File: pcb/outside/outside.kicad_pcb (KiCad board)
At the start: 2 copper layers, 56 parts, among them J1 USB_C_Receptacle_USB2.0_16P, J2 RJ12, J3 Conn_01x08, J4 Conn_01x04, Q1 NMOS, SW1 RST, SW2 PRG, U1 ESP32-C6-MINI-1, U2 MFRC52201HN1,157, U3 USBLC6-2P6, U4 AMS1117-3.3, Y1 XRCGB27M120F3M13R0

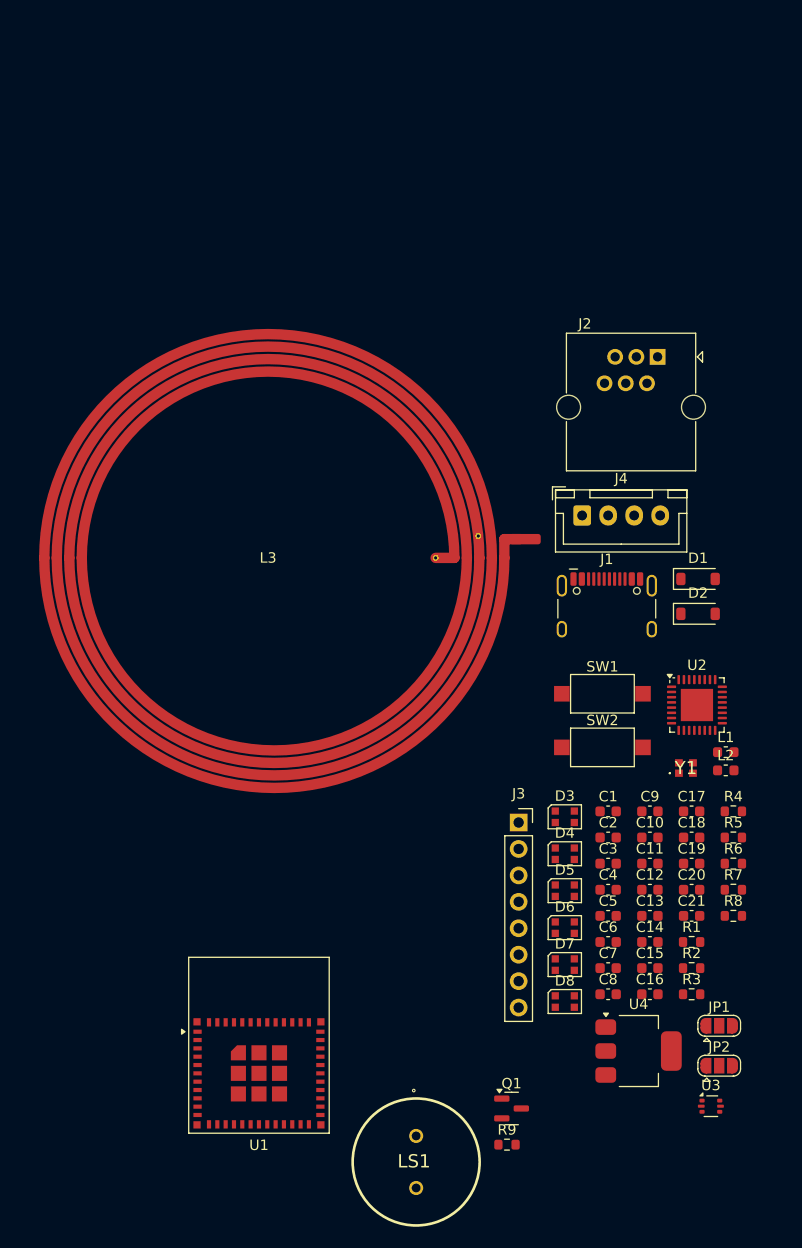
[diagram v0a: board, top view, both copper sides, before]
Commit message: feat: improve and rearrange schematic
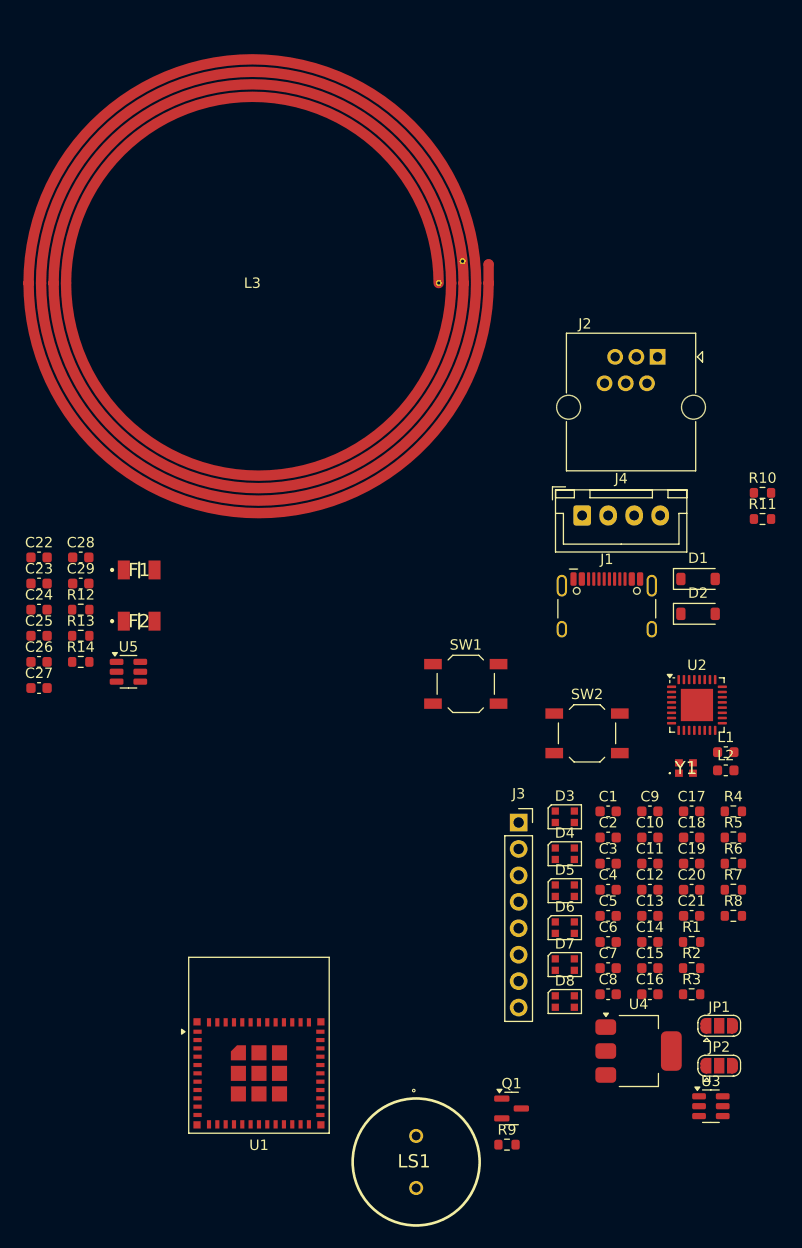
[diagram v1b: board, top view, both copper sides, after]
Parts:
- added C22: 100n, Capacitor_SMD:C_0603_1608Metric, F.Cu at (98.0, 76.5)
- added C23: 100n, Capacitor_SMD:C_0603_1608Metric, F.Cu at (98.0, 79.0)
- added C24: 100n, Capacitor_SMD:C_0603_1608Metric, F.Cu at (98.0, 81.5)
- added C25: 100n, Capacitor_SMD:C_0603_1608Metric, F.Cu at (98.0, 84.0)
- added C26: 100n, Capacitor_SMD:C_0603_1608Metric, F.Cu at (98.0, 86.5)
- added C27: 100n, Capacitor_SMD:C_0603_1608Metric, F.Cu at (98.0, 89.0)
- added C28: 100n, Capacitor_SMD:C_0603_1608Metric, F.Cu at (102.0, 76.5)
- added C29: 100n, Capacitor_SMD:C_0603_1608Metric, F.Cu at (102.0, 79.0)
- added F1: 500mA, belepteto:1206L05015YR, F.Cu at (107.6, 77.7)
- added F2: 500mA, belepteto:1206L05015YR, F.Cu at (107.6, 82.6)
- added R10: 5k1, Resistor_SMD:R_0603_1608Metric, F.Cu at (167.5, 70.3)
- added R11: 5k1, Resistor_SMD:R_0603_1608Metric, F.Cu at (167.5, 72.8)
- added R12: 180, Resistor_SMD:R_0603_1608Metric, F.Cu at (102.0, 81.5)
- added R13: 22, Resistor_SMD:R_0603_1608Metric, F.Cu at (102.0, 84.0)
- added R14: 22, Resistor_SMD:R_0603_1608Metric, F.Cu at (102.0, 86.5)
- added U5: USBLC6-2SC6, Package_TO_SOT_SMD:SOT-23-6, F.Cu at (106.6, 87.4)
- L1, L2: value 2.2uH -> 2u2
- L3: value 1.22uH -> 1u22
- LS1: value Speaker_Crystal -> PS1240P02BT
- Q1: value NMOS -> BSS138
- SW1, SW2: footprint Button_Switch_SMD:SW_SPST_CK_RS282G05A3 -> Button_Switch_SMD:SW_SPST_TL3342
- U3: value USBLC6-2P6 -> USBLC6-2SC6; footprint Package_TO_SOT_SMD:SOT-666 -> Package_TO_SOT_SMD:SOT-23-6
- Y1: value XRCGB27M120F3M13R0 -> 27.12MHz
- moved L3 26.4 mm to (118.5, 50.1)
- moved SW1 13.2 mm to (139.0, 88.6)
- moved SW2 2.00 mm to (150.6, 93.4)
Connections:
- net /EA renamed /RFID/EA
- net /I2C renamed /RFID/I2C
- net /IO2 renamed /ESP/SCLK
- net /IO3 renamed /ESP/MOSI
- net /IO4 renamed /ESP/MISO
- net /IO5 renamed /ESP/CS
- net /PRG renamed /ESP/PRG
- net Net-(J3-Pin_1) renamed /ESP/EXT_CS
- net Net-(J3-Pin_2) renamed /ESP/EXT_SCLK
- net Net-(J3-Pin_3) renamed /ESP/EXT_MOSI
- net Net-(J3-Pin_4) renamed /ESP/EXT_MISO
- net Net-(U2-OSCIN) renamed /RFID/OSC2
- net Net-(U2-OSCOUT) renamed /RFID/OSC1
- net Net-(U2-RX) renamed /RFID/RX
- net Net-(U2-TX1) renamed /RFID/TX1
- net Net-(U2-TX2) renamed /RFID/TX2
- net Net-(U2-VMID) renamed /RFID/VMID
- J1 pad A4: Net-(D1-A) -> Net-(F1-Pad1)
- J1 pad A9: Net-(D1-A) -> Net-(F1-Pad1)
- J1 pad B4: Net-(D1-A) -> Net-(F1-Pad1)
- J1 pad B9: Net-(D1-A) -> Net-(F1-Pad1)
- J2 pad 2: Net-(D2-A) -> Net-(F2-Pad1)
- J4 pad 2: /FPRINT_TX -> Net-(J4-Pin_2)
- J4 pad 3: /FPRINT_RX -> Net-(J4-Pin_3)
- Q1 pad 1: Net-(Q1-D) -> Net-(Q1-G)
- Q1 pad 2: /BUZZER -> GND
- Q1 pad 3: GND -> Net-(Q1-D)
- U1 pad 19: /BUZZER -> /ESP/BUZZER
- U1 pad 28: /FPRINT_RX -> /ESP/FPRINT_RX
- U1 pad 29: /FPRINT_TX -> /ESP/FPRINT_TX
- Y1 pad 2: unconnected-(Y1-NC_1-Pad2) -> GND
- Y1 pad 4: unconnected-(Y1-NC_2-Pad4) -> GND

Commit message: fix: USB polarity
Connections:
- U3 pad 4: /USB- -> /USB+
- U3 pad 6: /USB+ -> /USB-
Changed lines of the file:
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@@
 			(net 1 "GND")
 			(pinfunction "GND")
-			(pintype "power_out")
+			(pintype "passive")
 		)
 		(pad "A4" smd roundrect
@@
 			(net 29 "Net-(F1-Pad1)")
 			(pinfunction "VBUS")
-			(pintype "power_out")
+			(pintype "passive")
 		)
 		(pad "A5" smd roundrect
@@
 			(layers "F.Cu" "F.Mask" "F.Paste")
 			(roundrect_rratio 0.25)
-			(net 46 "/USB-")
+			(net 51 "/USB+")
 			(pinfunction "I/O2")
 			(pintype "passive")
@@
 			(layers "F.Cu" "F.Mask" "F.Paste")
 			(roundrect_rratio 0.25)
-			(net 51 "/USB+")
+			(net 46 "/USB-")
 			(pinfunction "I/O1")
 			(pintype "passive")

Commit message: feat: initial PCB
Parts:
- removed the C22 at (98.0, 76.5)
- removed the C25 at (98.0, 84.0)
- removed the C27 at (98.0, 89.0)
- removed the C28 at (102.0, 76.5)
- removed the C29 at (102.0, 79.0)
- removed the R12 at (102.0, 81.5)
- removed the R13 at (102.0, 84.0)
- removed the R14 at (102.0, 86.5)
- added C10: 100n, Capacitor_SMD:C_0603_1608Metric, F.Cu at (140.5, 28.5)
- added C13: 10u, Capacitor_SMD:C_0603_1608Metric, F.Cu at (126.5, 90.0)
- added C14: 100n, Capacitor_SMD:C_0603_1608Metric, F.Cu at (128.0, 90.0)
- added C15: 100n, Capacitor_SMD:C_0603_1608Metric, F.Cu at (134.8, 86.0)
- added C16: 10u, Capacitor_SMD:C_0603_1608Metric, F.Cu at (134.8, 84.5)
- added C18: 100n, Capacitor_SMD:C_0603_1608Metric, F.Cu at (148.0, 76.0)
- added C19: 100n, Capacitor_SMD:C_0603_1608Metric, F.Cu at (148.0, 77.5)
- added C20: 100n, Capacitor_SMD:C_0603_1608Metric, F.Cu at (143.0, 86.7)
- added C21: 100n, Capacitor_SMD:C_0603_1608Metric, F.Cu at (144.5, 86.7)
- added C9: 100n, Capacitor_SMD:C_0603_1608Metric, F.Cu at (109.2, 28.5)
- added G***: LOGO, belepteto:LEGO, F.Cu at (125.2, 39.0)
- added H1: MountingHole, MountingHole:MountingHole_3.2mm_M3, F.Cu at (103.5, 28.5)
- added H2: MountingHole, MountingHole:MountingHole_3.2mm_M3, F.Cu at (103.5, 96.5)
- added H3: MountingHole, MountingHole:MountingHole_3.2mm_M3, F.Cu at (146.5, 28.5)
- added H4: MountingHole, MountingHole:MountingHole_3.2mm_M3, F.Cu at (146.5, 96.5)
- added R6: 5k1, Resistor_SMD:R_0603_1608Metric, F.Cu at (118.5, 74.2)
- added R7: 5k1, Resistor_SMD:R_0603_1608Metric, F.Cu at (118.5, 72.8)
- added R8: 22, Resistor_SMD:R_0603_1608Metric, F.Cu at (142.2, 93.5)
- added TP1: BUZZER, TestPoint:TestPoint_Pad_D1.0mm, B.Cu at (117.5, 85.2)
- added TP10: OUT2, TestPoint:TestPoint_Pad_D1.0mm, B.Cu at (116.0, 79.0)
- added TP11: OUT1, TestPoint:TestPoint_Pad_D1.0mm, B.Cu at (118.5, 87.2)
- added TP12: EXT_MISO, TestPoint:TestPoint_Pad_D1.0mm, B.Cu at (130.2, 95.2)
- added TP13: EXT_MOSI, TestPoint:TestPoint_Pad_D1.0mm, B.Cu at (132.2, 94.8)
- added TP14: EXT_SCLK, TestPoint:TestPoint_Pad_D1.0mm, B.Cu at (134.2, 94.8)
- added TP15: EXT_CS, TestPoint:TestPoint_Pad_D1.0mm, B.Cu at (134.2, 92.6)
- added TP16: LED_IN, TestPoint:TestPoint_Pad_D1.0mm, B.Cu at (104.2, 60.8)
- added TP17: LED_OUT, TestPoint:TestPoint_Pad_D1.0mm, B.Cu at (134.8, 79.8)
- added TP18: FPRINT_RX, TestPoint:TestPoint_Pad_D1.0mm, B.Cu at (144.0, 94.5)
- added TP19: FPRINT_TX, TestPoint:TestPoint_Pad_D1.0mm, B.Cu at (134.5, 89.5)
- added TP2: ESP_RST, TestPoint:TestPoint_Pad_D1.0mm, B.Cu at (114.2, 98.5)
- added TP20: +5V, TestPoint:TestPoint_Pad_D1.0mm, B.Cu at (127.8, 86.5)
- added TP21: +3V3, TestPoint:TestPoint_Pad_D1.0mm, B.Cu at (131.8, 90.8)
- added TP22: GND, TestPoint:TestPoint_Pad_D1.0mm, B.Cu at (144.0, 98.5)
- added TP3: ESP_TX, TestPoint:TestPoint_Pad_D1.0mm, B.Cu at (109.5, 75.5)
- added TP4: ESP_RX, TestPoint:TestPoint_Pad_D1.0mm, B.Cu at (111.5, 75.5)
- added TP5: ESP_PRG, TestPoint:TestPoint_Pad_D1.0mm, B.Cu at (137.8, 82.8)
- added TP6: INT_CS, TestPoint:TestPoint_Pad_D1.0mm, B.Cu at (135.2, 84.0)
- added TP7: INT_SCLK, TestPoint:TestPoint_Pad_D1.0mm, B.Cu at (140.0, 84.0)
- added TP8: INT_MISO, TestPoint:TestPoint_Pad_D1.0mm, B.Cu at (137.5, 85.5)
- added TP9: INT_MOSI, TestPoint:TestPoint_Pad_D1.0mm, B.Cu at (142.2, 83.8)
- C1, C6: value 10u -> 100n
- C11, C12: value 15p -> 100n
- C23, C24: value 100n -> 15p
- C3: value 100n -> 10u
- C4: value 10u -> 1u
- C8: value 1u -> 100n
- J2, J4, LS1, SW1, SW2: moved to B.Cu
- R1: value 5k1 -> 1k
- R2: value 5k1 -> 180
- R9: value 1k -> 22
- U3: value USBLC6-2SC6 -> AMS1117-3.3; footprint Package_TO_SOT_SMD:SOT-23-6 -> Package_TO_SOT_SMD:SOT-223-3_TabPin2
- U4: value AMS1117-3.3 -> USBLC6-2SC6; footprint Package_TO_SOT_SMD:SOT-223-3_TabPin2 -> Package_TO_SOT_SMD:SOT-23-6
- moved C8 97.3 mm to (103.5, 34.5), turned to -90 degrees
- moved D5 90.9 mm to (109.2, 26.5), turned to 180 degrees
- moved D6 85.9 mm to (140.5, 26.5), turned to 180 degrees
- moved D4 84.7 mm to (101.5, 34.5), turned to -90 degrees
- moved D7 81.1 mm to (148.5, 34.5), turned to 90 degrees
- moved C7 73.7 mm to (103.5, 61.0), turned to -90 degrees
- moved C11 72.1 mm to (146.5, 34.5), turned to 90 degrees
- moved U4 68.2 mm to (111.6, 71.8)
- moved D3 62.0 mm to (101.5, 61.0), turned to -90 degrees
- moved D8 58.1 mm to (148.5, 61.0), turned to 90 degrees
- moved R3 56.0 mm to (119.5, 80.5), turned to 180 degrees
- moved R5 55.1 mm to (110.5, 93.7), turned to 90 degrees
- moved R2 52.4 mm to (119.5, 83.5)
- moved C34 51.0 mm to (142.5, 69.4), turned to 90 degrees
- moved C25 49.6 mm to (130.9, 71.2), turned to 180 degrees
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- renumbered C10 to C17, C9 to C22, C21 to C25, C15 to C27, C13 to C28, C17 to C29, C19 to C30, C14 to C31, C18 to C32, C20 to C33, C16 to C34, R11 to R10, R10 to R11, R6 to R12, R7 to R13, R8 to R14
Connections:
- net /ESP/CS renamed /CS
- net /ESP/EXT_CS renamed /EXT_CS
- net /ESP/EXT_MISO renamed /EXT_MISO
- net /ESP/EXT_MOSI renamed /EXT_MOSI
- net /ESP/EXT_SCLK renamed /EXT_SCLK
- net /ESP/FPRINT_RX renamed /FPRINT_RX
- net /ESP/FPRINT_TX renamed /FPRINT_TX
- net /ESP/MISO renamed /MISO
- net /ESP/MOSI renamed /MOSI
- net /ESP/SCLK renamed /SCLK
- net Net-(U2-NRSTPD) renamed /RFID/RST
- C1 pad 1: +5V -> +3V3
- C11 pad 1: /RFID/OSC2 -> GND
- C11 pad 2: GND -> +5V
- C12 pad 1: /RFID/OSC1 -> GND
- C12 pad 2: GND -> +5V
- C2 pad 1: +5V -> +3V3
- C23 pad 1: GND -> /RFID/OSC2
- C23 pad 2: /RST -> GND
- C24 pad 1: GND -> /RFID/OSC1
- C24 pad 2: +5V -> GND
- C26 pad 1: GND -> /RFID/VMID
- C26 pad 2: +5V -> GND
- C4 pad 1: GND -> /RST
- C4 pad 2: +3V3 -> GND
- C5 pad 2: +3V3 -> /RST
- C6 pad 1: +3V3 -> GND
- C6 pad 2: GND -> /PRG
- C7 pad 1: +3V3 -> GND
- C7 pad 2: GND -> +5V
- C8 pad 1: /RST -> GND
- C8 pad 2: GND -> +5V
- J1 pad A5: Net-(J1-CC1) -> /USB_CC1
- J1 pad A6: Net-(J1-D+-PadA6) -> /USBC+
- J1 pad A7: Net-(J1-D--PadA7) -> /USBC-
- J1 pad B5: Net-(J1-CC2) -> /USB_CC2
- J1 pad B6: Net-(J1-D+-PadA6) -> /USBC+
- J1 pad B7: Net-(J1-D--PadA7) -> /USBC-
- R1 pad 1: Net-(J1-CC1) -> +5V
- R1 pad 2: GND -> Net-(Q1-D)
- R2 pad 1: Net-(J1-CC2) -> /BUZZER
- R2 pad 2: GND -> Net-(Q1-G)
- R3 pad 2: /RST -> /PRG
- R4 pad 2: /ESP/PRG -> /LED_IN
- R5 pad 2: /LED_IN -> /RST
- R9 pad 1: +5V -> Net-(J4-Pin_2)
- R9 pad 2: Net-(Q1-D) -> Net-(R9-Pad2)
- SW2 pad 2: /ESP/PRG -> /PRG
- U1 pad 19: /ESP/BUZZER -> /BUZZER
- U1 pad 23: /ESP/PRG -> /PRG
- U1 pad 30: unconnected-(U1-RXD0-Pad30) -> Net-(U1-RXD0)
- U1 pad 31: unconnected-(U1-TXD0-Pad31) -> Net-(U1-TXD0)
- U2 pad 12: unconnected-(U2-TVDD-Pad12) -> +3V3
- U2 pad 9: unconnected-(U2-SVDD-Pad9) -> +3V3
- U3 pad 1: Net-(J1-D--PadA7) -> GND
- U3 pad 2: GND -> +3V3
- U3 pad 3: Net-(J1-D+-PadA6) -> +5V
- U4 pad 1: GND -> /USBC-
- U4 pad 2: +3V3 -> GND
- U4 pad 3: +5V -> /USBC+
- U5 pad 3: Net-(R14-Pad2) -> Net-(R9-Pad2)
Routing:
- net GND: track 0.00 -> 201.6 mm, vias 0 -> 90
- net +5V: track 0.00 -> 200.0 mm, vias 0 -> 8
- net +3V3: track 0.00 -> 111.6 mm, vias 0 -> 6
- net /FPRINT_RX: track 0.00 -> 53.3 mm, vias 0 -> 2
- net /PRG: track 0.00 -> 51.4 mm, vias 0 -> 3
- net /EXT_CS: track 0.00 -> 49.8 mm, vias 0 -> 2
- net /EXT_SCLK: track 0.00 -> 49.0 mm, vias 0 -> 2
- net /FPRINT_TX: track 0.00 -> 46.9 mm, vias 0 -> 2
- net /MISO: track 0.00 -> 45.5 mm, vias 0 -> 4
- net /MOSI: track 0.00 -> 43.8 mm, vias 0 -> 4
- net /SCLK: track 0.00 -> 43.7 mm, vias 0 -> 4
- net /LED_OUT: track 0.00 -> 43.3 mm, vias 0 -> 2
- net /RST: track 0.00 -> 41.2 mm, vias 0 -> 5
- net /EXT_MOSI: track 0.00 -> 39.9 mm, vias 0 -> 2
- net /CS: track 0.00 -> 38.3 mm, vias 0 -> 4
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- added copper zone on F.Cu, net +3V3
- added copper zone on B.Cu, net GND
- added copper zone on F.Cu, net GND
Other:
- board outline added: 50 x 75 mm
- board text added: "Beléptető"
- board text added: "https://github.com/legokor/belepteto"
